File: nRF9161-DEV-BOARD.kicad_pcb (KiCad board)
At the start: 4 copper layers, 120 x 80 mm, 104 parts, among them J1 VIN_3V0-5V5, J10 SPI0, J11 I2C0, J12 GPIO_P0.00-15, J13 GPIO_P0.16-31, J14 RFFE_MAGPIO, J15 COEX, J16 I2S, J17 PDM, J18 ADC_AIN0-7, J2 U.FL_LTE_NR+, J3 SWF_LTE, J5 U.FL_GNSS, J6 SWF_GNSS, J7 nanoSIM_4FF, J8 SWD_10pin, J9 UART0, SW1 DISABLE, SW2 RESET, SW3 USER, U1 NRF9161-LACA-R7, U2 TLV73333PDBV, U3 TPS22919DCKR, U4 TPD3F303DPV

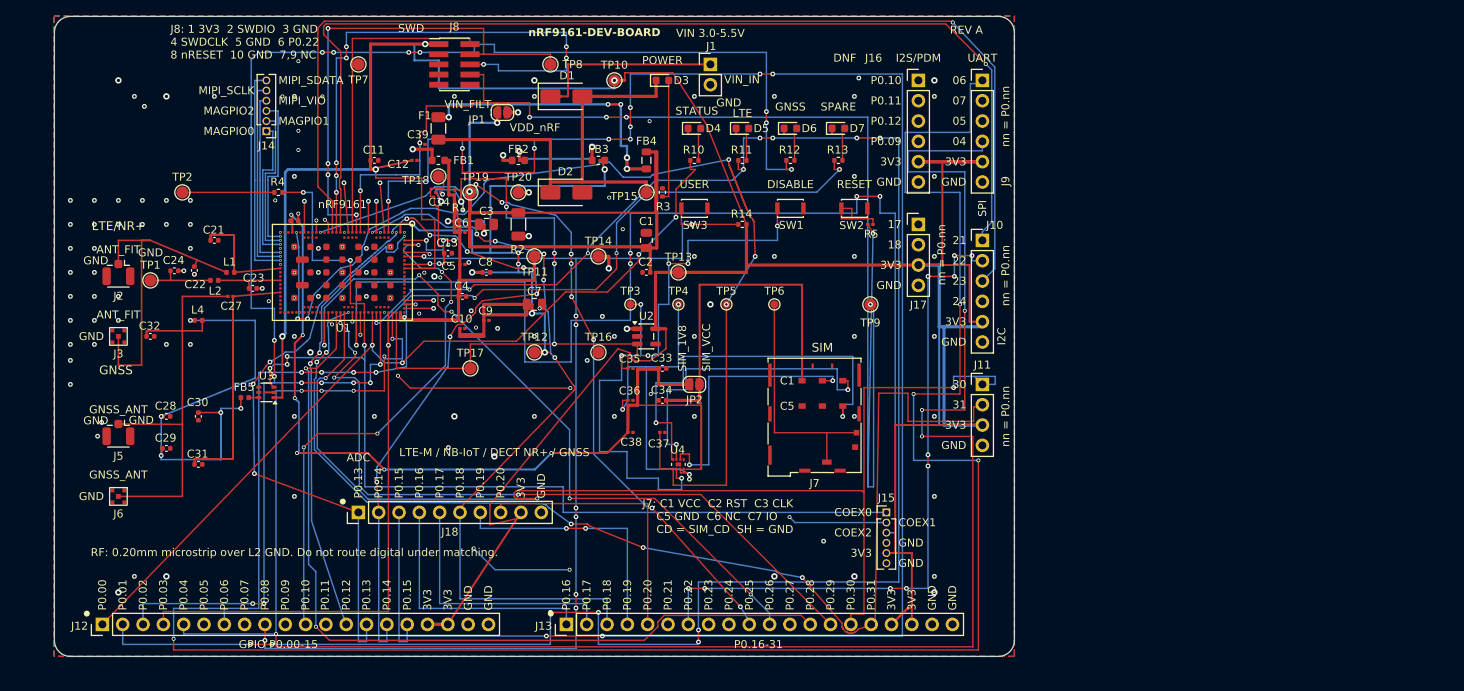
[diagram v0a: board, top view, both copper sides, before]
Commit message: v2 layout 1: update PCB from schematic 0dc7f09 (remove J1,J3,J6,J9-J18,JP1,R2,R4,R11-R14,D5-D7,SW1,SW3,TP2-6,10-12,18-20; add U5-U8,Q1,R21,R23,C41-C48,J20; pad nets synced, dead-net copper removed)
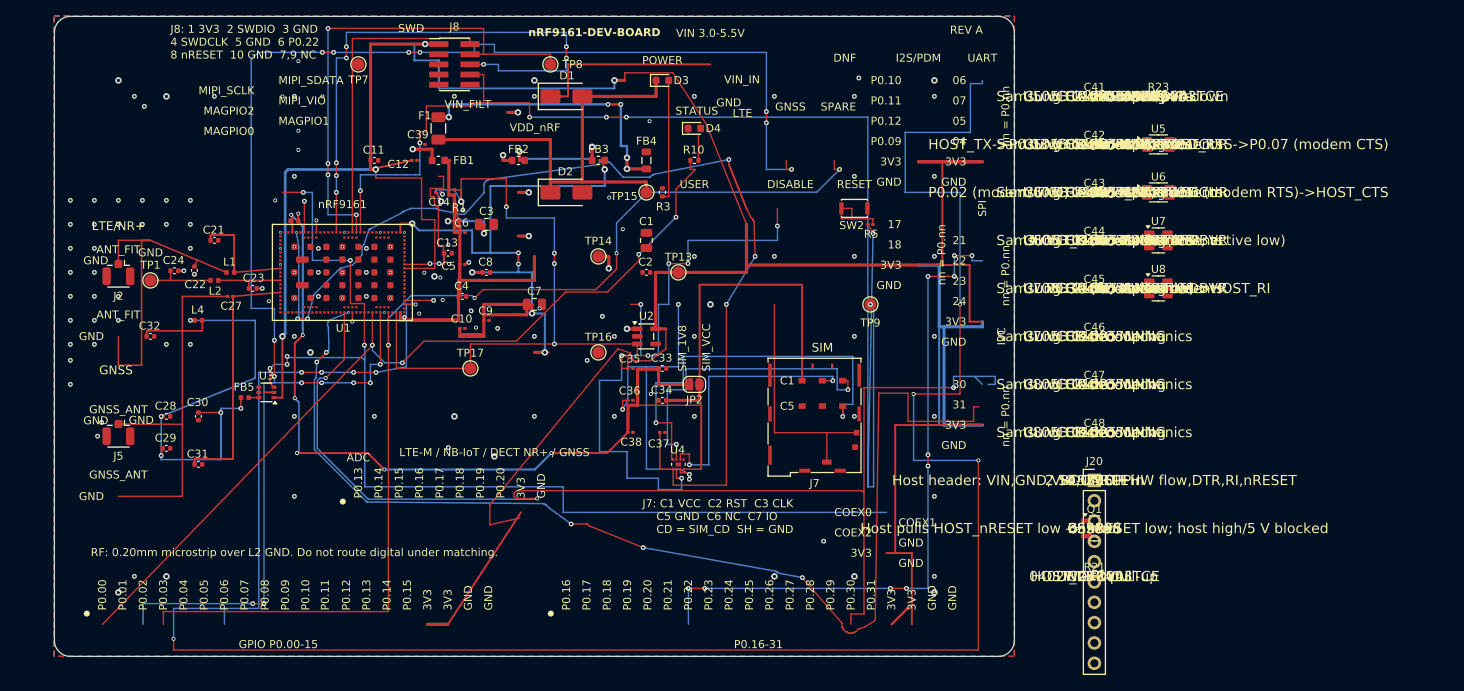
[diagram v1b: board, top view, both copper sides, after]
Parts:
- removed D5, D6, D7: Green LED, LED_SMD:LED_0603_1608Metric
- removed J1: VIN_3V0-5V5, Connector_PinHeader_2.54mm:PinHeader_1x02_P2.54mm_Vertical
- removed J10: SPI0, Connector_PinHeader_2.54mm:PinHeader_1x06_P2.54mm_Vertical
- removed J11: I2C0, Connector_PinHeader_2.54mm:PinHeader_1x04_P2.54mm_Vertical
- removed J12: GPIO_P0.00-15, Connector_PinHeader_2.54mm:PinHeader_1x20_P2.54mm_Vertical
- removed J13: GPIO_P0.16-31, Connector_PinHeader_2.54mm:PinHeader_1x20_P2.54mm_Vertical
- removed J14: RFFE_MAGPIO, Connector_PinHeader_1.27mm:PinHeader_1x06_P1.27mm_Vertical
- removed J15: COEX, Connector_PinHeader_1.27mm:PinHeader_1x06_P1.27mm_Vertical
- removed J16: I2S, Connector_PinHeader_2.54mm:PinHeader_1x06_P2.54mm_Vertical
- removed J17: PDM, Connector_PinHeader_2.54mm:PinHeader_1x04_P2.54mm_Vertical
- removed J18: ADC_AIN0-7, Connector_PinHeader_2.54mm:PinHeader_1x10_P2.54mm_Vertical
- removed J3: SWF_LTE, Board:Murata_MM8130-2600_SWF
- removed J6: SWF_GNSS, Board:Murata_MM8130-2600_SWF
- removed J9: UART0, Connector_PinHeader_2.54mm:PinHeader_1x06_P2.54mm_Vertical
- removed JP1: I_MEAS, Jumper:SolderJumper-2_P1.3mm_Open_RoundedPad1.0x1.5mm
- removed R11, R12, R13: 1k, Resistor_SMD:R_0402_1005Metric
- removed R14: 10k, Resistor_SMD:R_0402_1005Metric
- removed R2: 0.05, Resistor_SMD:R_1206_3216Metric
- removed R4: 0R, Resistor_SMD:R_0402_1005Metric
- removed SW1: DISABLE, Button_Switch_SMD:SW_SPST_CK_KXT3
- removed SW3: USER, Button_Switch_SMD:SW_SPST_CK_KXT3
- removed TP10: VDD_GPIO, TestPoint:TestPoint_Pad_D1.5mm
- removed TP11: VDD1, TestPoint:TestPoint_Pad_D1.5mm
- removed TP12: VDD2, TestPoint:TestPoint_Pad_D1.5mm
- removed TP18: DEC0, TestPoint:TestPoint_Pad_D1.5mm
- removed TP19: I_MEAS+, TestPoint:TestPoint_Pad_D1.5mm
- removed TP2: LNA_EN, TestPoint:TestPoint_Pad_D1.5mm
- removed TP20: I_MEAS-, TestPoint:TestPoint_Pad_D1.5mm
- removed TP3: SIM_CLK, TestPoint:TestPoint_Pad_D1.0mm
- removed TP4: SIM_RST, TestPoint:TestPoint_Pad_D1.0mm
- removed TP5: SIM_IO, TestPoint:TestPoint_Pad_D1.0mm
- removed TP6: SIM_CD, TestPoint:TestPoint_Pad_D1.0mm
- added C41: 100nF, Capacitor_SMD:C_0402_1005Metric, F.Cu at (130.0, 10.0)
- added C42: 100nF, Capacitor_SMD:C_0402_1005Metric, F.Cu at (130.0, 16.0)
- added C43: 100nF, Capacitor_SMD:C_0402_1005Metric, F.Cu at (130.0, 22.0)
- added C44: 100nF, Capacitor_SMD:C_0402_1005Metric, F.Cu at (130.0, 28.0)
- added C45: 100nF, Capacitor_SMD:C_0402_1005Metric, F.Cu at (130.0, 34.0)
- added C46: 100nF, Capacitor_SMD:C_0402_1005Metric, F.Cu at (130.0, 40.0)
- added C47: 100nF, Capacitor_SMD:C_0402_1005Metric, F.Cu at (130.0, 46.0)
- added C48: 100nF, Capacitor_SMD:C_0402_1005Metric, F.Cu at (130.0, 52.0)
- added J20: HOST_1x10_2.54, Connector_PinHeader_2.54mm:PinHeader_1x10_P2.54mm_Vertical, F.Cu at (130.0, 58.0)
- added Q1: BSS138, Package_TO_SOT_SMD:SOT-23, F.Cu at (130.0, 64.0)
- added R21: 100k, Resistor_SMD:R_0402_1005Metric, F.Cu at (130.0, 70.0)
- added R23: 100k, Resistor_SMD:R_0402_1005Metric, F.Cu at (138.0, 10.0)
- added U5: SN74LXC2T45, Package_SO:VSSOP-8_2.3x2mm_P0.5mm, F.Cu at (138.0, 16.0)
- added U6: SN74LXC2T45, Package_SO:VSSOP-8_2.3x2mm_P0.5mm, F.Cu at (138.0, 22.0)
- added U7: SN74LXC1T45, Package_TO_SOT_SMD:SOT-23-6, F.Cu at (138.0, 28.0)
- added U8: SN74LXC1T45, Package_TO_SOT_SMD:SOT-23-6, F.Cu at (138.0, 34.0)
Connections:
- C1 pad 1: VIN_FILT -> VDD_nRF
- C2 pad 1: VIN_FILT -> VDD_nRF
- FB4 pad 2: VIN_FILT -> VDD_nRF
- J7 pad C6: (no net) -> unconnected-(J7-VPP/SWP-PadC6)
- J8 pad 7: (no net) -> unconnected-(J8-Pin_7-Pad7)
- J8 pad 9: (no net) -> unconnected-(J8-Pin_9-Pad9)
- U1 pad 10: (no net) -> unconnected-(U1E-RES-Pad10)
- U1 pad 100: P0.04 -> unconnected-(U1C-P0.04-Pad100)
- U1 pad 104: (no net) -> unconnected-(U1E-RES-Pad104)
- U1 pad 105: (no net) -> unconnected-(U1E-RES-Pad105)
- U1 pad 106: (no net) -> unconnected-(U1E-RES-Pad106)
- U1 pad 107: (no net) -> unconnected-(U1E-RES-Pad107)
- U1 pad 108: (no net) -> unconnected-(U1E-RES-Pad108)
- U1 pad 109: (no net) -> unconnected-(U1E-RES-Pad109)
- U1 pad 110: (no net) -> unconnected-(U1E-RES-Pad110)
- U1 pad 111: (no net) -> unconnected-(U1E-RES-Pad111)
- U1 pad 112: (no net) -> unconnected-(U1E-RES-Pad112)
- U1 pad 113: (no net) -> unconnected-(U1E-RES-Pad113)
- U1 pad 114: (no net) -> unconnected-(U1E-RES-Pad114)
- U1 pad 115: (no net) -> unconnected-(U1E-RES-Pad115)
- U1 pad 116: (no net) -> unconnected-(U1E-RES-Pad116)
- U1 pad 117: (no net) -> unconnected-(U1E-RES-Pad117)
- U1 pad 118: (no net) -> unconnected-(U1E-RES-Pad118)
- U1 pad 119: (no net) -> unconnected-(U1E-RES-Pad119)
- U1 pad 120: (no net) -> unconnected-(U1E-RES-Pad120)
- U1 pad 121: (no net) -> unconnected-(U1E-RES-Pad121)
- U1 pad 122: (no net) -> unconnected-(U1E-RES-Pad122)
- U1 pad 123: (no net) -> unconnected-(U1E-RES-Pad123)
- U1 pad 124: (no net) -> unconnected-(U1E-RES-Pad124)
- U1 pad 125: (no net) -> unconnected-(U1E-RES-Pad125)
- U1 pad 126: (no net) -> unconnected-(U1E-RES-Pad126)
- U1 pad 127: (no net) -> unconnected-(U1E-RES-Pad127)
- U1 pad 15: P0.08 -> unconnected-(U1C-P0.08-Pad15)
- U1 pad 16: P0.09 -> unconnected-(U1C-P0.09-Pad16)
- U1 pad 18: P0.10 -> unconnected-(U1C-P0.10-Pad18)
- U1 pad 19: P0.11 -> unconnected-(U1C-P0.11-Pad19)
- U1 pad 2: P0.05 -> unconnected-(U1C-P0.05-Pad2)
- U1 pad 20: P0.12 -> unconnected-(U1C-P0.12-Pad20)
- U1 pad 23: P0.13 -> unconnected-(U1C-P0.13_AIN0-Pad23)
- U1 pad 24: P0.14 -> unconnected-(U1C-P0.14_AIN1-Pad24)
- U1 pad 25: P0.15 -> unconnected-(U1C-P0.15_AIN2-Pad25)
- U1 pad 26: P0.16 -> unconnected-(U1D-P0.16_AIN3-Pad26)
- U1 pad 28: P0.17 -> unconnected-(U1D-P0.17_AIN4-Pad28)
- U1 pad 29: P0.18 -> unconnected-(U1D-P0.18_AIN5-Pad29)
- U1 pad 30: P0.19 -> unconnected-(U1D-P0.19_AIN6-Pad30)
- U1 pad 35: P0.20 -> unconnected-(U1D-P0.20_AIN7-Pad35)
- U1 pad 37: P0.21 -> unconnected-(U1D-P0.21_TRACECLK-Pad37)
- U1 pad 39: P0.23 -> unconnected-(U1D-P0.23_TRACEDATA1-Pad39)
- U1 pad 40: P0.24 -> unconnected-(U1D-P0.24_TRACEDATA2-Pad40)
- U1 pad 42: P0.25 -> unconnected-(U1D-P0.25_TRACEDATA3-Pad42)
- U1 pad 45: (no net) -> unconnected-(U1E-SIM_DET-Pad45)
- U1 pad 51: (no net) -> unconnected-(U1E-RES-Pad51)
- U1 pad 53: MAGPIO2 -> unconnected-(U1B-MAGPIO2-Pad53)
- U1 pad 54: MAGPIO1 -> unconnected-(U1B-MAGPIO1-Pad54)
- U1 pad 55: MAGPIO0 -> unconnected-(U1B-MAGPIO0-Pad55)
- U1 pad 57: MIPI_VIO -> unconnected-(U1B-MIPI_VIO-Pad57)
- U1 pad 58: MIPI_SCLK -> unconnected-(U1B-MIPI_SCLK-Pad58)
- U1 pad 59: MIPI_SDATA -> unconnected-(U1B-MIPI_SDATA-Pad59)
- U1 pad 70: (no net) -> unconnected-(U1E-RES-Pad70)
- U1 pad 71: (no net) -> unconnected-(U1E-RES-Pad71)
- U1 pad 73: (no net) -> unconnected-(U1E-RES-Pad73)
- U1 pad 83: P0.26 -> unconnected-(U1D-P0.26-Pad83)
- U1 pad 84: P0.27 -> unconnected-(U1D-P0.27-Pad84)
- U1 pad 86: P0.28 -> unconnected-(U1D-P0.28-Pad86)
- U1 pad 87: P0.29 -> unconnected-(U1D-P0.29-Pad87)
- U1 pad 91: COEX2 -> unconnected-(U1B-COEX2-Pad91)
- U1 pad 92: COEX1 -> unconnected-(U1B-COEX1-Pad92)
- U1 pad 96: P0.01 -> unconnected-(U1C-P0.01-Pad96)
- U2 pad 4: (no net) -> unconnected-(U2-NC-Pad4)
- U3 pad 4: (no net) -> unconnected-(U3-NC-Pad4)
- U3 pad 5: (no net) -> unconnected-(U3-QOD-Pad5)
- U4 pad 4: (no net) -> unconnected-(U4-NC-Pad4)
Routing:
- net P0.01: track 251.8 -> 0.00 mm, vias 14 -> 0
- net P0.04: track 250.6 -> 0.00 mm, vias 9 -> 0
- net P0.15: track 244.8 -> 0.00 mm, vias 11 -> 0
- net P0.21: track 198.9 -> 0.00 mm, vias 1 -> 0
- net P0.23: track 198.7 -> 0.00 mm, vias 1 -> 0
- net P0.18: track 159.0 -> 0.00 mm, vias 6 -> 0
- net P0.17: track 155.9 -> 0.00 mm, vias 1 -> 0
- net COEX2: track 153.2 -> 0.00 mm, vias 5 -> 0
- net P0.24: track 150.5 -> 0.00 mm, vias 1 -> 0
- net P0.08: track 140.2 -> 0.00 mm, vias 9 -> 0
- net P0.28: track 106.8 -> 0.00 mm, vias 2 -> 0
- net P0.20: track 105.7 -> 0.00 mm, vias 1 -> 0
- net P0.05: track 98.0 -> 0.00 mm, vias 1 -> 0
- net P0.25: track 93.8 -> 0.00 mm, vias 9 -> 0
- net VIN_FILT: track 93.7 -> 0.00 mm, vias 2 -> 0
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
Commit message: v2 layout 2: 50x34 mm outline, two-sided placement; RF keepouts B1-B5 as B.Cu rule areas (B6 n/a, no on-board antenna), In1 no-track rule area; 0.20 mm RF feeds hand-routed (J2/J5 within 10 mm)
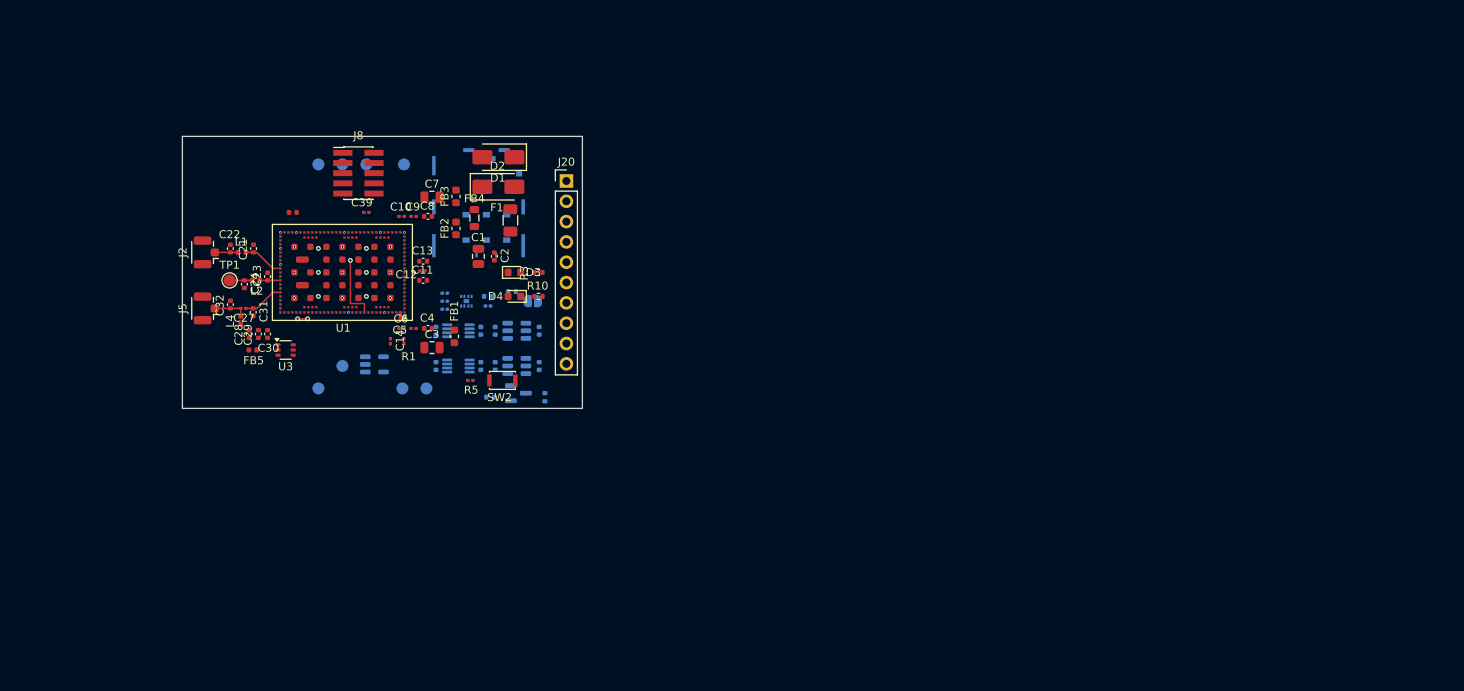
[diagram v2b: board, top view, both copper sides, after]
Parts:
- C33, C34, C35, C36, C37, C38, C41, C42, C43, C44, C45, C46, C47, C48, J7, JP2, Q1, R21, R23, TP13, TP14, TP15, TP16, TP17, TP7, TP8, TP9, U2, U4, U5, U6, U7, U8: moved to B.Cu
- moved R23 91.6 mm to (54.5, 47.6)
- moved U5 90.5 mm to (50.5, 39.3)
- moved U6 90.2 mm to (50.5, 43.7)
- moved C41 87.4 mm to (47.7, 39.3), turned to 90 degrees
- moved C43 85.1 mm to (47.7, 43.7), turned to 90 degrees
- moved U7 81.0 mm to (57.8, 39.3)
- moved U8 80.8 mm to (57.8, 43.7)
- moved C42 80.2 mm to (53.3, 39.3), turned to 90 degrees
- moved C44 78.3 mm to (53.3, 43.7), turned to 90 degrees
- moved J20 75.9 mm to (64.0, 20.6)
- moved C45 75.1 mm to (55.1, 39.3), turned to 90 degrees
- moved C47 74.9 mm to (55.1, 43.7), turned to 90 degrees
- moved Q1 74.0 mm to (58.0, 47.1)
- moved R21 72.3 mm to (61.3, 47.6), turned to 90 degrees
- moved C48 69.9 mm to (60.6, 43.7), turned to 90 degrees
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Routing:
- net VDD_GPIO: track 426.1 -> 0.00 mm, vias 4 -> 0
- net P0.06: track 278.4 -> 0.00 mm, vias 9 -> 0
- net P0.22: track 211.4 -> 0.00 mm, vias 18 -> 0
- net P0.02: track 198.3 -> 0.00 mm, vias 16 -> 0
- net nRESET: track 190.0 -> 0.00 mm, vias 7 -> 0
- net P0.30: track 148.7 -> 0.00 mm, vias 3 -> 0
- net P0.31: track 144.5 -> 0.00 mm, vias 6 -> 1
- net P0.03: track 140.0 -> 0.00 mm, vias 4 -> 0
- net SIM_IO: track 134.4 -> 1.25 mm, vias 6 -> 3
- net SIM_RST: track 128.9 -> 0.00 mm, vias 5 -> 0
- net COEX0: track 131.3 -> 8.25 mm, vias 6 -> 1
- net ENABLE: track 121.9 -> 0.00 mm, vias 10 -> 0
- net SIM_1V8: track 114.9 -> 0.00 mm, vias 6 -> 0
- net SIM_CLK: track 114.9 -> 0.00 mm, vias 4 -> 0
- net P0.00: track 108.6 -> 0.00 mm, vias 4 -> 0
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- removed copper zone on B.Cu, net GND
- removed copper zone on F.Cu, net GND
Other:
- board size 120 x 80 mm -> 50 x 34 mm
- board text removed: "04"
- board text removed: "05"
- board text removed: "06"
- board text removed: "07"
- board text removed: "17"
- board text removed: "18"
- board text removed: "21"
- board text removed: "22"
- board text removed: "23"
- board text removed: "24"
- board text removed: "30"
- board text removed: "31"
- board text removed: "3V3"
- board text removed: "ADC"
- board text removed: "ANT_FIT"
- board text removed: "C1"
- board text removed: "C5"
- board text removed: "COEX0"
- board text removed: "COEX1"
- board text removed: "COEX2"
- board text removed: "DISABLE"
- board text removed: "DNF"
- board text removed: "GND"
- board text removed: "GNSS"
- board text removed: "GNSS_ANT"
- board text removed: "GPIO P0.00-15"
- board text removed: "I2C"
- board text removed: "I2S/PDM"
- board text removed: "J7: C1 VCC C2 RST C3 CLK C5 GND C6 NC C7 IO CD = SIM_CD SH = GND"
- board text removed: "J8: 1 3V3 2 SWDIO 3 GND 4 SWDCLK 5 GND 6 P0.22 8 nRESET 10 GND 7,9 NC"
- board text removed: "LTE"
- board text removed: "LTE-M / NB-IoT / DECT NR+ / GNSS"
- board text removed: "LTE/NR+"
- board text removed: "MAGPIO0"
- board text removed: "MAGPIO1"
- board text removed: "MAGPIO2"
- board text removed: "MIPI_SCLK"
- board text removed: "MIPI_SDATA"
- board text removed: "MIPI_VIO"
- board text removed: "P0.00"
- board text removed: "P0.01"
- board text removed: "P0.02"
- board text removed: "P0.03"
- board text removed: "P0.04"
- board text removed: "P0.05"
- board text removed: "P0.06"
- board text removed: "P0.07"
- board text removed: "P0.08"
- board text removed: "P0.09"
- board text removed: "P0.10"
- board text removed: "P0.11"
- board text removed: "P0.12"
- board text removed: "P0.13"
- board text removed: "P0.14"
- board text removed: "P0.15"
- board text removed: "P0.16"
- board text removed: "P0.16-31"
- board text removed: "P0.17"
- board text removed: "P0.18"
- board text removed: "P0.19"
- board text removed: "P0.20"
- board text removed: "P0.21"
- board text removed: "P0.22"
- board text removed: "P0.23"
- board text removed: "P0.24"
- board text removed: "P0.25"
- board text removed: "P0.26"
- board text removed: "P0.27"
- board text removed: "P0.28"
- board text removed: "P0.29"
- board text removed: "P0.30"
- board text removed: "P0.31"
- board text removed: "POWER"
- board text removed: "RESET"
- board text removed: "REV A"
- board text removed: "RF: 0.20mm microstrip over L2 GND. Do not route digital under matching."
- board text removed: "SIM"
- board text removed: "SIM_1V8"
- board text removed: "SIM_VCC"
- board text removed: "SPARE"
- board text removed: "SPI"
- board text removed: "STATUS"
- board text removed: "SWD"
- board text removed: "UART"
- board text removed: "USER"
- board text removed: "VDD_nRF"
- board text removed: "VIN 3.0-5.5V"
- board text removed: "VIN_FILT"
- board text removed: "VIN_IN"
- board text removed: "VIPPO: IPC-4761 Type VII filled+capped, 29 pl.: 0.20/0.30 x20 (U1 pads 20,21,23,24,27,29,36,42,48,52-60,89,98), 0.25/0.40 x9 (U1 pad 103)"
- board text removed: "nRF9161"
- board text removed: "nRF9161-DEV-BOARD"
- board text removed: "nn = P0.nn"
